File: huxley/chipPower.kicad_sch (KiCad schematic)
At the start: 23 parts, among them J1 CT3151V1-2, J2 CT3151V1-2, J3 CT3151V1-2, J34 CT3151V1-0, J35 CT3151V1-2, J37 CT3151V1-0

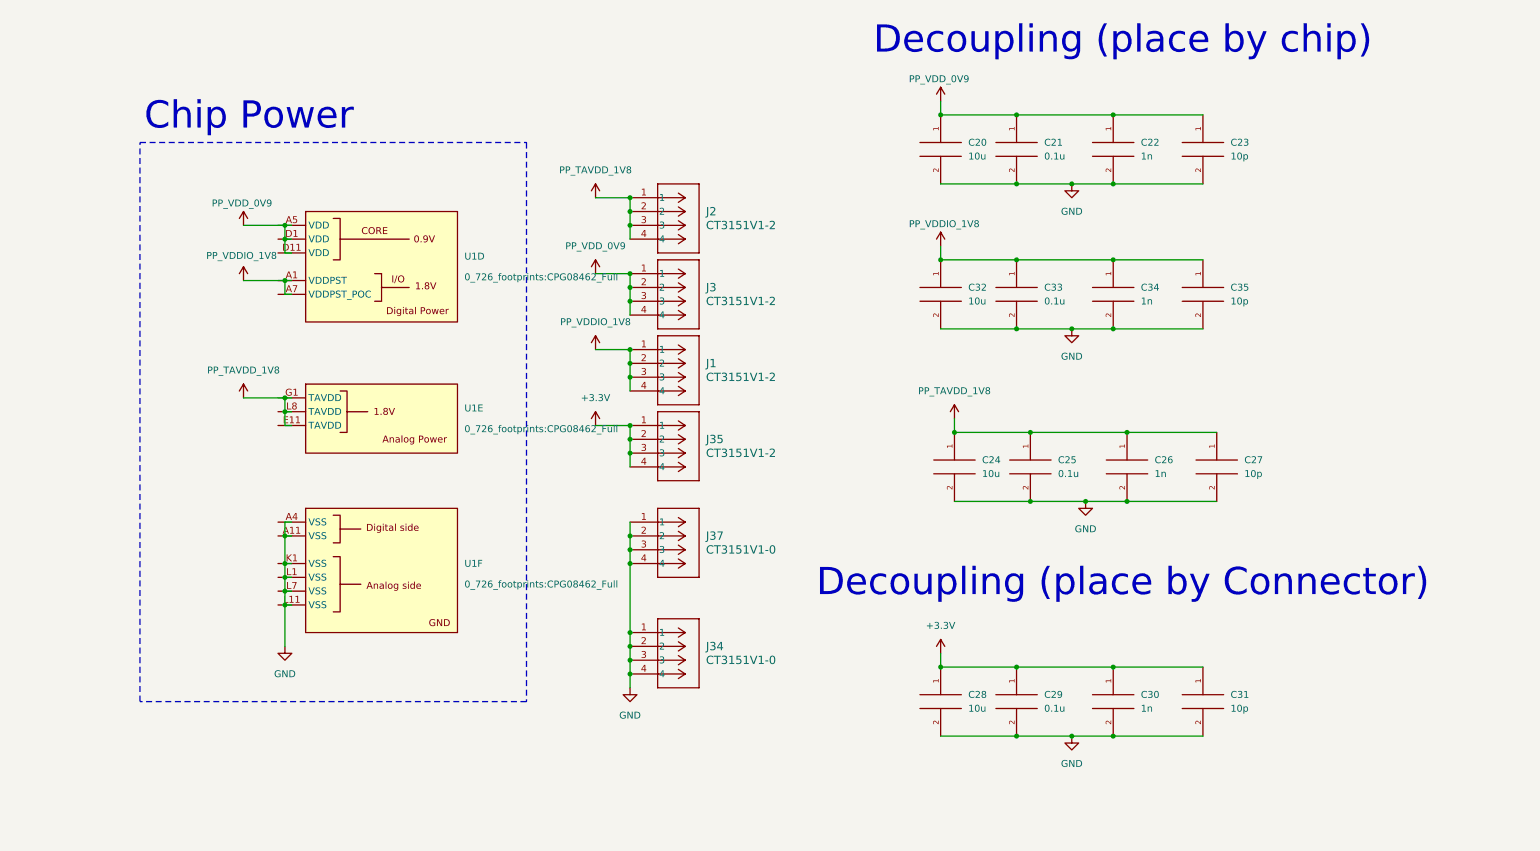
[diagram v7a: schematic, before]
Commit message: reorganized pin assignment to level shifter; matched 3V3 power net name; minor schematic cleanup
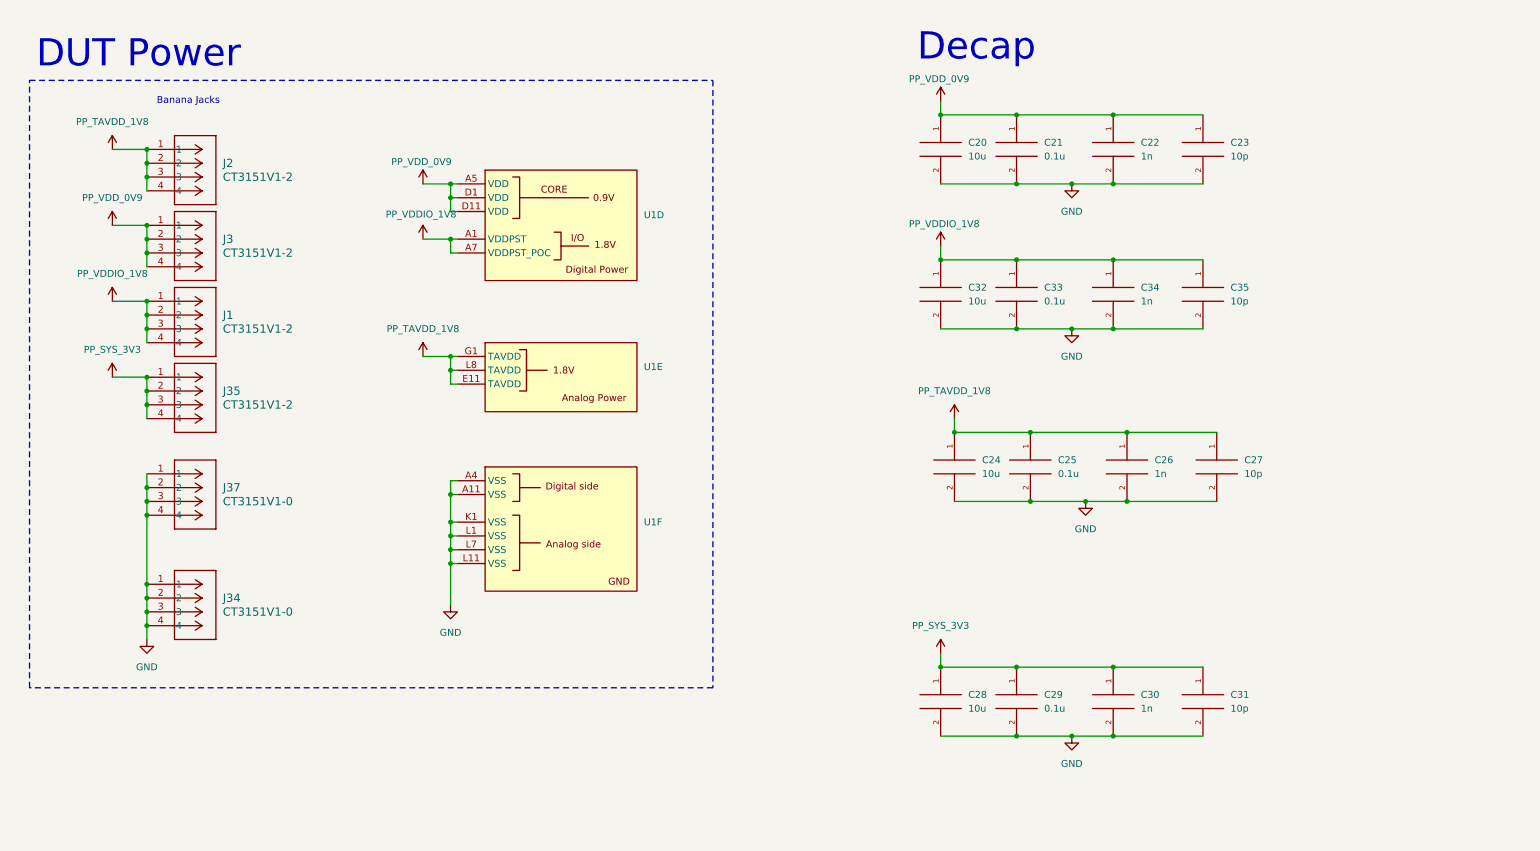
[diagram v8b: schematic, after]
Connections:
- net GND: now also U1.A11 (VSS), U1.A4 (VSS), U1.K1 (VSS), U1.L1 (VSS), U1.L11 (VSS), U1.L7 (VSS)
- net PP_TAVDD_1V8: now also U1.E11 (TAVDD), U1.G1 (TAVDD), U1.L8 (TAVDD)
- net PP_VDDIO_1V8: now also U1.A1 (VDDPST), U1.A7 (VDDPST_POC)
- net PP_VDD_0V9: now also U1.A5 (VDD), U1.D1 (VDD), U1.D11 (VDD)
- net +3.3V renamed PP_SYS_3V3
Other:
- note added: "Banana Jacks"
- note added: "DUT Power"
- note added: "Decap"
- note removed: "Chip Power"
- note removed: "Decoupling (place by Connector)"
- note removed: "Decoupling (place by chip)"
- moved on the sheet: J1, J2, J3, J34, J35, J37, U1D, U1E, U1F
